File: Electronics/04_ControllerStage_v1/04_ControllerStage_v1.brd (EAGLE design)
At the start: 100 x 80 mm, 43 parts, among them J1 SCREW_TERMINAL_4, J2 BARRIER_BLOCK-4PIN, J3 CONN_2X3_SMD, U1 XL4005-DEV

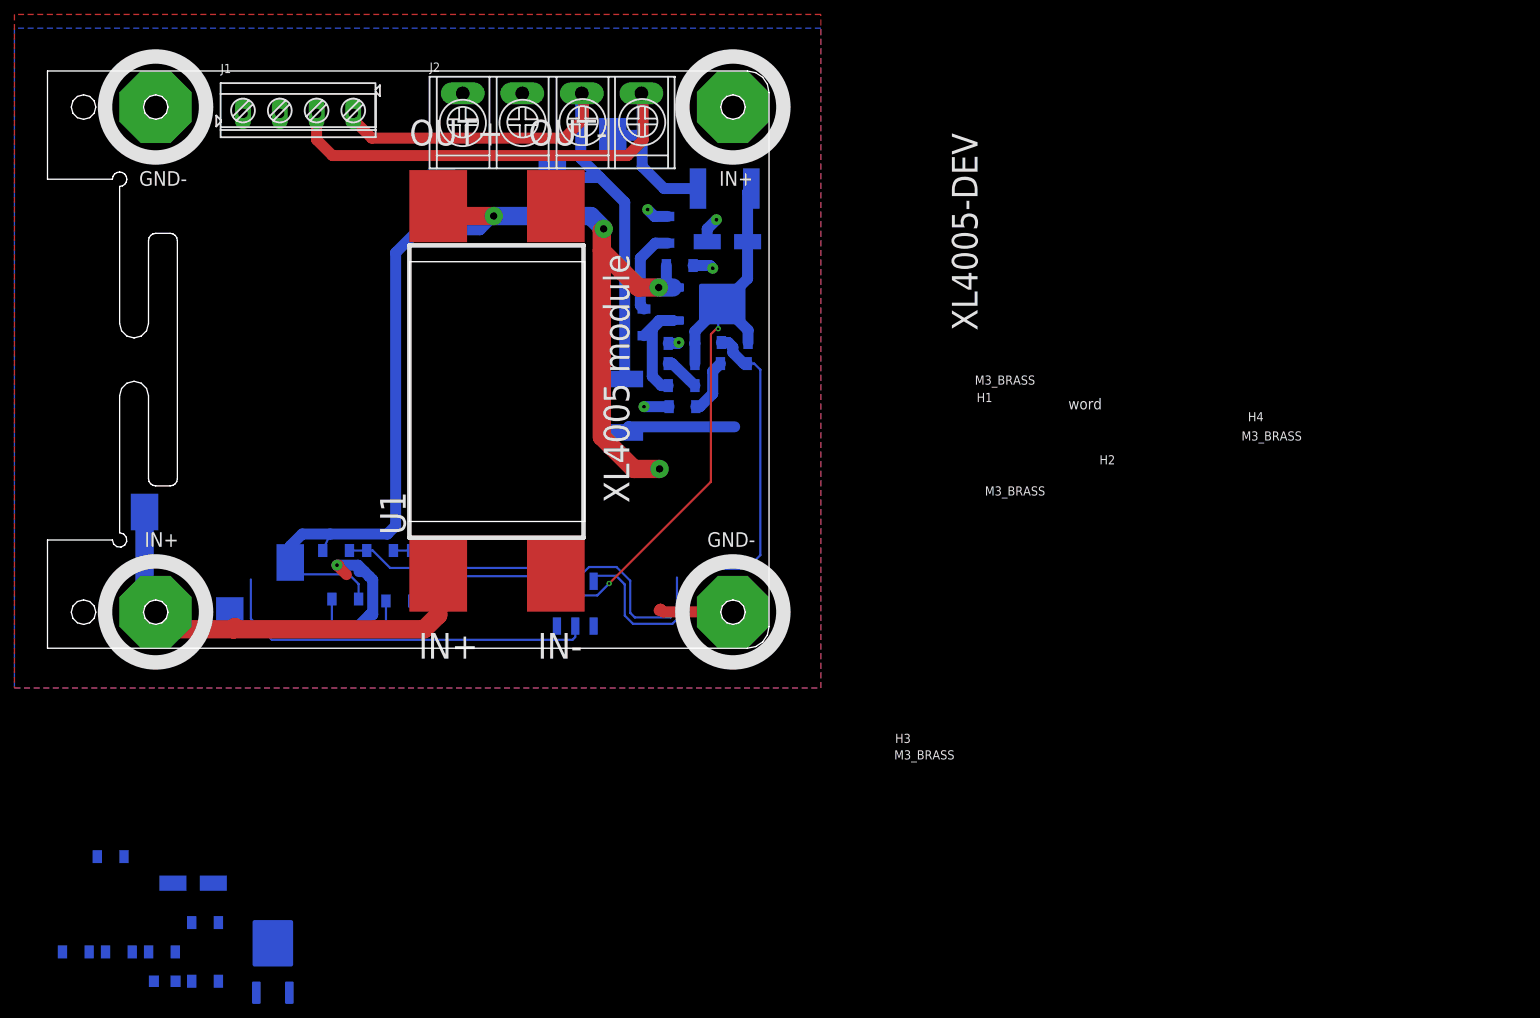
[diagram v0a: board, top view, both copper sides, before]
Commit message: Components and values determined on schematic and routing started on controller stage
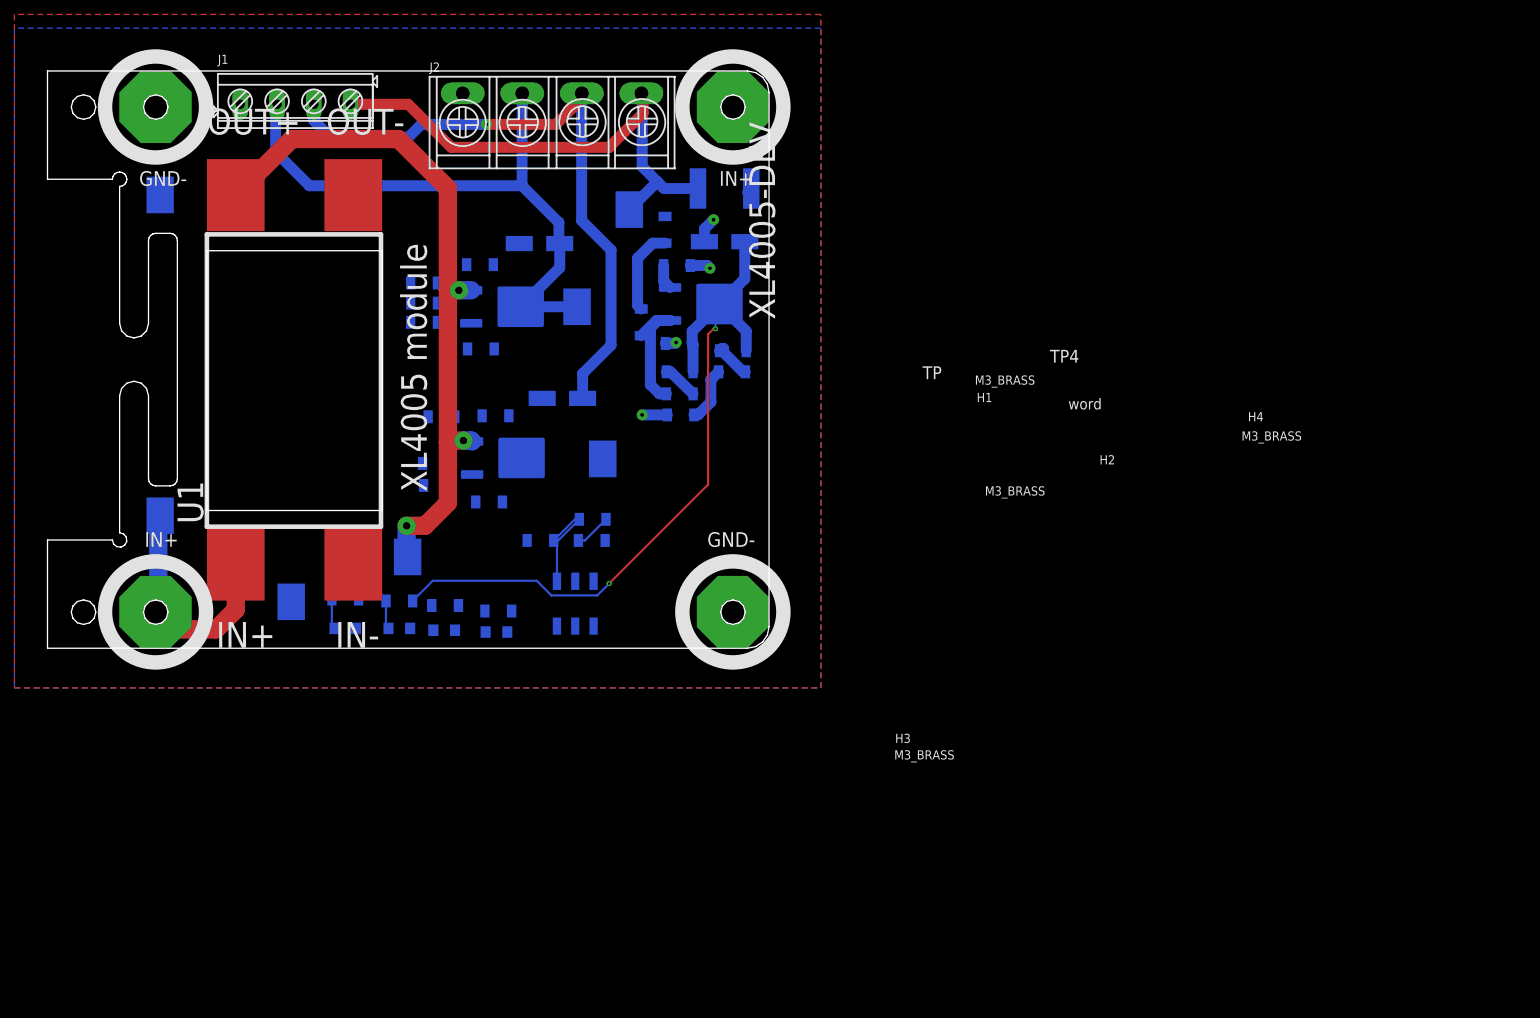
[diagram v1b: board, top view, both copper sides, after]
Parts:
- removed F1: PTC, Hippo-PS:PTC
- removed TP8: TP, Hippo-PS:TP
- added C5: 10 uF, standardparts:1206
- added C6: 22 uF, standardparts:1206
- added D4: YELLOW, standardparts:1206.LED
- added R2: AZ1117CDAZ1117CD, Hippo-PS:AZ1117CD
- added R3: 1K, standardparts:1206
- added R4: 10K, standardparts:1206
- added R5: 4.7K, standardparts:1206
- added R6: 220, standardparts:1206
- added TP5, TP6: TP, Hippo-PS:TP
- added U$2: 100 uF, Hippo-PS:ELECTROLYTIC_CAP
- R10, R22: value 330 -> 220
- R18: value 470 -> 100
- R20, R8: value 6.8K -> 10K
- R21, R9: value 6.8K -> 4.7K
- R7: value 10K -> 1K
- moved R9 104.5 mm to (69.5, 68.8)
- moved U$1 100.8 mm to (85.5, 74.3), turned to 180 degrees
- moved R7 97.0 mm to (69.5, 66.0)
- moved R8 97.0 mm to (69.5, 63.4)
- moved C3 96.7 mm to (77.2, 71.4)
- moved R1 96.2 mm to (80.3, 65.5), turned to 90 degrees
- moved C4 88.2 mm to (77.3, 59.7)
- moved D1 62.2 mm to (72.3, 20.7)
- moved R10 61.8 mm to (72.4, 24.1)
- moved TP2 39.0 mm to (32.9, 81.0)
- moved R25 29.8 mm to (92.8, 36.1)
- moved R24 28.4 mm to (85.6, 33.1)
- moved U1 28.1 mm to (39.4, 34.8)
- moved R26 23.2 mm to (92.7, 33.1)
- moved TP3 16.3 mm to (67.2, 30.9)
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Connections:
- removed net N$17: F1.1, J1.P$4, J2.P$3, TP8.P$1
- new net N$2: D4.P$1, R6.2
- new net N$3: R4.1, R5.2
- new net OUT3: C6.2, J1.P$3, J2.P$3, R2.2, R3.2, R6.1, TP6.P$1, U$2.+
- new net SIG3: R3.1, R4.2
- net GND: now also C5.1, C6.1, D4.P$2, R2.1, R5.1, U$2.-
- net N$18: now also J1.P$4; no longer J1.P$3
- net OUT1: now also C2.2, F2.2, R14.2, R15.1, R19.2, R22.1, U$3.+; no longer F1.2
- net OUT2: now also J1.P$2, J2.P$2, TP5.P$1; no longer C2.2, F2.2, R14.2, R15.1, R19.2, R22.1, U$3.+
- net SIG1: now also R19.1, R20.2
- net SIG2: no longer R19.1, R20.2
- net V+: now also C5.2, R2.3
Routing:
- net OUT1: track 15.8 -> 105.0 mm, vias 0 -> 2
- net OUT3: track 0.00 -> 88.9 mm, vias 0 -> 1
- net N$17: track 87.5 -> 0.00 mm
- net SIG2: track 67.5 -> 0.87 mm
- net V+: track 165.6 -> 108.4 mm, vias 4 -> 3
- net SIG_NP: track 53.3 -> 0.00 mm
- net GND: track 45.9 -> 11.5 mm, vias 6 -> 4
- net IN+: track 61.4 -> 33.6 mm
- net OUT2: track 111.3 -> 84.6 mm, vias 2 -> 0
- net SIG1: track 25.5 -> 5.41 mm
- net SIG_SMPS: track 30.7 -> 14.6 mm
- net N$18: track 80.6 -> 72.5 mm
- net N$9: track 2.69 -> 5.21 mm
- net N$12: track 17.5 -> 18.6 mm

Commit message: Finish routing controller stage electronics
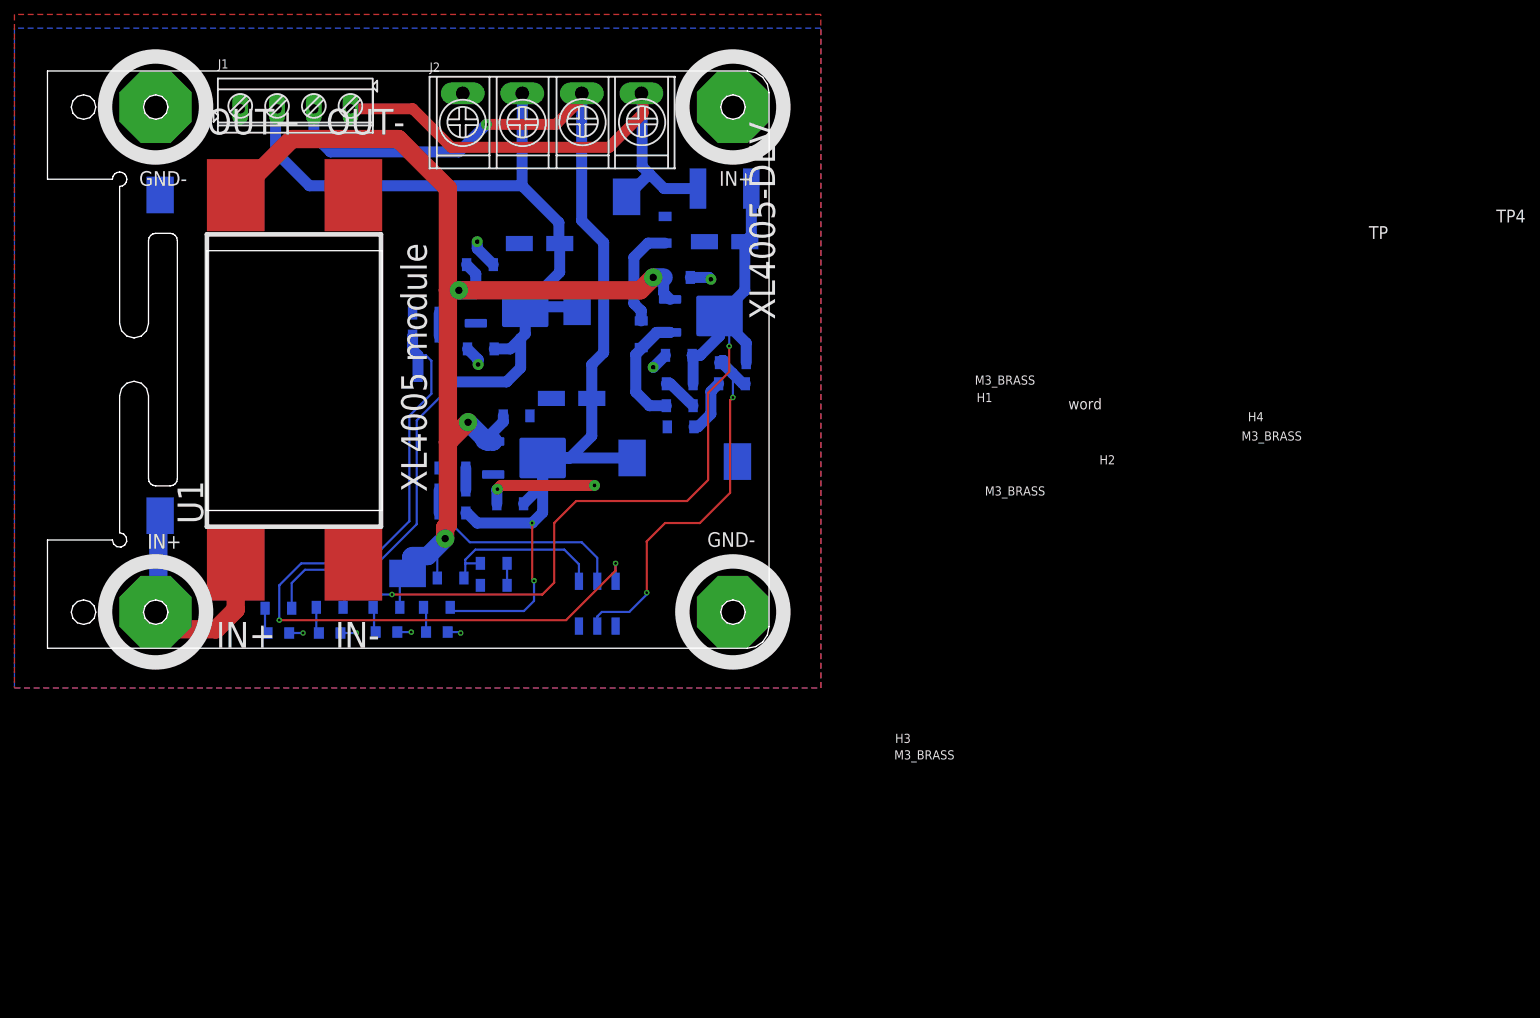
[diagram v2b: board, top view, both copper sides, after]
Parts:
- moved TP4 64.8 mm to (112.9, 44.1)
- moved R10 23.1 mm to (49.3, 23.7)
- moved D1 23.0 mm to (49.3, 20.3), turned to 180 degrees
- moved R25 15.0 mm to (79.1, 30.0)
- moved R26 14.9 mm to (79.1, 26.9), turned to 0 degrees
- moved R24 13.5 mm to (73.2, 27.9)
- moved R7 10.1 mm to (70.5, 56.0), turned to 180 degrees
- moved R22 9.69 mm to (56.4, 23.9)
- moved D2 9.67 mm to (56.4, 20.3)
- moved R6 8.52 mm to (71.2, 23.9)
- moved D4 8.25 mm to (71.2, 20.4), turned to 180 degrees
- moved R5 7.27 mm to (73.4, 43.2), turned to 180 degrees
- moved R23 5.83 mm to (64.3, 23.9)
- moved D3 5.74 mm to (64.3, 20.4)
- moved R3 4.38 mm to (73.4, 37.0), turned to 180 degrees
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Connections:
- removed net SIG_NP: J3.4
- net SIG1: now also J3.4; no longer J3.3
- net SIG3: now also J3.3
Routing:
- net SIG2: track 0.87 -> 110.9 mm, vias 0 -> 2
- net OUT3: track 88.9 -> 165.6 mm, vias 1 -> 3
- net OUT2: track 84.6 -> 153.6 mm
- net V+: track 108.4 -> 160.9 mm, vias 3 -> 4
- net SIG1: track 5.41 -> 53.3 mm, vias 0 -> 2
- net SIG3: track 0.00 -> 30.9 mm
- net GND: track 11.5 -> 35.8 mm, vias 4 -> 10
- net OUT1: track 105.0 -> 126.9 mm
- net SIG_SMPS: track 14.6 -> 24.3 mm
- net N$1: track 0.00 -> 3.57 mm
- net N$2: track 0.00 -> 3.57 mm
- net N$5: track 0.00 -> 3.17 mm
- net N$3: track 0.00 -> 3.05 mm
- net N$12: track 18.6 -> 21.1 mm
- net N$13: track 11.9 -> 14.4 mm
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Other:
- board text added: "ek robotgrrl Jul 16, '22"
- board text added: "hippo-pd contrllr v1"
- board text removed: "ek robotgrrl Jul 13, '22"
- board text removed: "hippo-ps sbc v1"
